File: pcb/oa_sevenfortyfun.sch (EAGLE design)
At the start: 33 parts, among them Q1 2N3904, Q10 2N3904, Q11 2N3904, Q12 2N3904, Q13 2N3904, Q14 2N3904, Q15 2N3906, Q16 2N3904, Q17 2N3906, Q18 2N3906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

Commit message: updating
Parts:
- added J1, J2, J3, J4, J5, J6, J7, J8: 1X01, Ai_Connectors:1X01
- added STANDOFF1, STANDOFF2, STANDOFF3, STANDOFF4: STAND-OFF, Ai_Electromechanical:STAND-OFF
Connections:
- removed net OFFSET1: Q6.E, R1.1
- removed net OFFSET2: Q7.E, R2.1
- new net NC: J8.1
- new net OFFSET_N1: J1.1, Q6.E, R1.1
- new net OFFSET_N2: J5.1, Q7.E, R2.1
- net IN+: now also J3.1
- net IN-: now also J2.1
- net OUT: now also J6.1
- net VCC+: now also J7.1
- net VCC-: now also J4.1
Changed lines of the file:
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@@
 <part name="R11" library="Ai_Passives" deviceset="RES" device="AXIAL-0.4"/>
 <part name="Q15" library="Ai_DiscreteSemis" deviceset="TRANSISTOR-PNP" device="" value="2N3906"/>
+<part name="STANDOFF1" library="Ai_Electromechanical" deviceset="STAND-OFF" device=""/>
+<part name="STANDOFF2" library="Ai_Electromechanical" deviceset="STAND-OFF" device=""/>
+<part name="STANDOFF3" library="Ai_Electromechanical" deviceset="STAND-OFF" device=""/>
+<part name="STANDOFF4" library="Ai_Electromechanical" deviceset="STAND-OFF" device=""/>
+<part name="J1" library="Ai_Connectors" deviceset="1X01" device=""/>
+<part name="J2" library="Ai_Connectors" deviceset="1X01" device=""/>
+<part name="J3" library="Ai_Connectors" deviceset="1X01" device=""/>
+<part name="J4" library="Ai_Connectors" deviceset="1X01" device=""/>
+<part name="J5" library="Ai_Connectors" deviceset="1X01" device=""/>
+<part name="J6" library="Ai_Connectors" deviceset="1X01" device=""/>
+<part name="J7" library="Ai_Connectors" deviceset="1X01" device=""/>
+<part name="J8" library="Ai_Connectors" deviceset="1X01" device=""/>
 </parts>
 <sheets>
@@
 <wire x1="168.91" y1="142.24" x2="168.91" y2="50.8" width="0.4064" layer="94" style="dashdot"/>
 <text x="62.23" y="144.78" size="1.778" layer="94" font="vector" ratio="15">DIFFERENTIAL AMPLIFIER</text>
-<text x="102.87" y="144.78" size="1.778" layer="94" font="vector" ratio="15">BIAS GENERATOR</text>
+<text x="106.68" y="144.78" size="1.778" layer="94" font="vector" ratio="15">BIAS GENERATOR</text>
 <text x="143.51" y="144.78" size="1.778" layer="94" font="vector" ratio="15">GAIN STAGE</text>
 <text x="171.45" y="144.78" size="1.778" layer="94" font="vector" ratio="15">OUTPUT STAGE</text>
@@
 <instance part="R11" gate="G$1" x="186.69" y="91.44" rot="R270"/>
 <instance part="Q15" gate="G$1" x="184.15" y="77.47" rot="MR0"/>
+<instance part="STANDOFF1" gate="G$1" x="132.08" y="2.54"/>
+<instance part="STANDOFF2" gate="G$1" x="137.16" y="2.54"/>
+<instance part="STANDOFF3" gate="G$1" x="142.24" y="2.54"/>
+<instance part="STANDOFF4" gate="G$1" x="127" y="2.54"/>
+<instance part="J1" gate="G$1" x="83.82" y="40.64" rot="R270"/>
+<instance part="J2" gate="G$1" x="107.95" y="40.64" rot="R270"/>
+<instance part="J3" gate="G$1" x="133.35" y="40.64" rot="R270"/>
+<instance part="J4" gate="G$1" x="158.75" y="40.64" rot="R270"/>
+<instance part="J5" gate="G$1" x="167.64" y="158.75" rot="R90"/>
+<instance part="J6" gate="G$1" x="146.05" y="158.75" rot="R90"/>
+<instance part="J7" gate="G$1" x="116.84" y="158.75" rot="R90"/>
+<instance part="J8" gate="G$1" x="90.17" y="158.75" rot="R90"/>
 </instances>
 <busses>
@@
 </segment>
 </net>
-<net name="OFFSET2" class="0">
+<net name="OFFSET_N2" class="0">
 <segment>
 <pinref part="Q7" gate="G$1" pin="E"/>
@@
 <label x="53.34" y="69.85" size="1.27" layer="95" font="vector" ratio="15" rot="R180" xref="yes"/>
 </segment>
-</net>
-<net name="OFFSET1" class="0">
-<segment>
-<pinref part="Q6" gate="G$1" pin="E"/>
-<pinref part="R1" gate="G$1" pin="1"/>
-<wire x1="64.77" y1="76.2" x2="64.77" y2="74.93" width="0.1524" layer="91"/>
-<wire x1="64.77" y1="74.93" x2="64.77" y2="68.58" width="0.1524" layer="91"/>
-<wire x1="64.77" y1="74.93" x2="53.34" y2="74.93" width="0.1524" layer="91"/>
-<junction x="64.77" y="74.93"/>
-<label x="53.34" y="74.93" size="1.27" layer="95" font="vector" ratio="15" rot="R180" xref="yes"/>
+<segment>
+<pinref part="J5" gate="G$1" pin="1"/>
+<wire x1="167.64" y1="163.83" x2="167.64" y2="166.37" width="0.1524" layer="91"/>
+<label x="167.64" y="166.37" size="1.27" layer="95" font="vector" ratio="15" rot="R90" xref="yes"/>
 </segment>
 </net>
@@
 <label x="53.34" y="116.84" size="1.27" layer="95" font="vector" ratio="15" rot="R180" xref="yes"/>
 </segment>
+<segment>
+<pinref part="J3" gate="G$1" pin="1"/>
+<wire x1="133.35" y1="35.56" x2="133.35" y2="33.02" width="0.1524" layer="91"/>
+<label x="133.35" y="33.02" size="1.27" layer="95" font="vector" ratio="15" rot="R270" xref="yes"/>
+</segment>
 </net>
 <net name="IN-" class="0">
@@
 <wire x1="96.52" y1="110.49" x2="53.34" y2="110.49" width="0.1524" layer="91"/>
 <label x="53.34" y="110.49" size="1.27" layer="95" font="vector" ratio="15" rot="R180" xref="yes"/>
+</segment>
+<segment>
+<pinref part="J2" gate="G$1" pin="1"/>
+<wire x1="107.95" y1="35.56" x2="107.95" y2="33.02" width="0.1524" layer="91"/>
+<label x="107.95" y="33.02" size="1.27" layer="95" font="vector" ratio="15" rot="R270" xref="yes"/>
 </segment>
 </net>
@@
 <junction x="186.69" y="85.09"/>
 <label x="196.85" y="85.09" size="1.27" layer="95" font="vector" ratio="15" xref="yes"/>
+</segment>
+<segment>
+<pinref part="J6" gate="G$1" pin="1"/>
+<wire x1="146.05" y1="163.83" x2="146.05" y2="166.37" width="0.1524" layer="91"/>
+<label x="146.05" y="166.37" size="1.27" layer="95" font="vector" ratio="15" rot="R90" xref="yes"/>
 </segment>
 </net>
@@
 <label x="53.34" y="54.61" size="1.27" layer="95" font="vector" ratio="15" rot="R180" xref="yes"/>
 </segment>
+<segment>
+<pinref part="J4" gate="G$1" pin="1"/>
+<wire x1="158.75" y1="35.56" x2="158.75" y2="33.02" width="0.1524" layer="91"/>
+<label x="158.75" y="33.02" size="1.27" layer="95" font="vector" ratio="15" rot="R270" xref="yes"/>
+</segment>
 </net>
 <net name="VCC+" class="0">
@@
 <label x="53.34" y="137.16" size="1.27" layer="95" font="vector" ratio="15" rot="R180" xref="yes"/>
 </segment>
-</net>
+<segment>
+<pinref part="J7" gate="G$1" pin="1"/>
+<wire x1="116.84" y1="163.83" x2="116.84" y2="166.37" width="0.1524" layer="91"/>
+<label x="116.84" y="166.37" size="1.27" layer="95" font="vector" ratio="15" rot="R90" xref="yes"/>
+</segment>
+</net>
+<net name="OFFSET_N1" class="0">
+<segment>
+<pinref part="J1" gate="G$1" pin="1"/>
+<wire x1="83.82" y1="35.56" x2="83.82" y2="33.02" width="0.1524" layer="91"/>
+<label x="83.82" y="33.02" size="1.27" layer="95" font="vector" ratio="15" rot="R270" xref="yes"/>
+</segment>
+<segment>
+<pinref part="Q6" gate="G$1" pin="E"/>
+<pinref part="R1" gate="G$1" pin="1"/>
+<wire x1="64.77" y1="76.2" x2="64.77" y2="74.93" width="0.1524" layer="91"/>
+<wire x1="64.77" y1="74.93" x2="64.77" y2="68.58" width="0.1524" layer="91"/>
+<wire x1="64.77" y1="74.93" x2="53.34" y2="74.93" width="0.1524" layer="91"/>
+<junction x="64.77" y="74.93"/>
+<label x="53.34" y="74.93" size="1.27" layer="95" font="vector" ratio="15" rot="R180" xref="yes"/>
+</segment>
+</net>
+<net name="NC" class="0">
+<segment>
+<pinref part="J8" gate="G$1" pin="1"/>
+<wire x1="90.17" y1="163.83" x2="90.17" y2="166.37" width="0.1524" layer="91"/>
+<label x="90.17" y="166.37" size="1.27" layer="95" font="vector" ratio="15" rot="R90" xref="yes"/>
+</segment>
+</net>

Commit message: Working on silkscreen
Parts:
- added J9: 2X04, Ai_Connectors:2X04
- J1, J2, J3, J4, J5, J6, J7, J8: value 1X01 -> 1X01-TERM; device Ai_Connectors:1X01 -> Ai_Connectors:1X01-TERM
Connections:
- net IN+: now also J9.5
- net IN-: now also J9.3
- net NC: now also J9.2
- net OFFSET_N1: now also J9.1
- net OFFSET_N2: now also J9.8
- net OUT: now also J9.6
- net VCC+: now also J9.4
- net VCC-: now also J9.7
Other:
- note added: "BREAKOUT"
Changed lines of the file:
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@@
 <?xml version="1.0" encoding="utf-8"?>
 <!DOCTYPE eagle SYSTEM "eagle.dtd">
-<eagle version="6.6.0">
+<eagle version="7.1.0">
 <drawing>
 <settings>
@@
 <part name="STANDOFF3" library="Ai_Electromechanical" deviceset="STAND-OFF" device=""/>
 <part name="STANDOFF4" library="Ai_Electromechanical" deviceset="STAND-OFF" device=""/>
-<part name="J1" library="Ai_Connectors" deviceset="1X01" device=""/>
-<part name="J2" library="Ai_Connectors" deviceset="1X01" device=""/>
-<part name="J3" library="Ai_Connectors" deviceset="1X01" device=""/>
-<part name="J4" library="Ai_Connectors" deviceset="1X01" device=""/>
-<part name="J5" library="Ai_Connectors" deviceset="1X01" device=""/>
-<part name="J6" library="Ai_Connectors" deviceset="1X01" device=""/>
-<part name="J7" library="Ai_Connectors" deviceset="1X01" device=""/>
-<part name="J8" library="Ai_Connectors" deviceset="1X01" device=""/>
+<part name="J1" library="Ai_Connectors" deviceset="1X01-TERM" device=""/>
+<part name="J2" library="Ai_Connectors" deviceset="1X01-TERM" device=""/>
+<part name="J3" library="Ai_Connectors" deviceset="1X01-TERM" device=""/>
+<part name="J4" library="Ai_Connectors" deviceset="1X01-TERM" device=""/>
+<part name="J5" library="Ai_Connectors" deviceset="1X01-TERM" device=""/>
+<part name="J6" library="Ai_Connectors" deviceset="1X01-TERM" device=""/>
+<part name="J7" library="Ai_Connectors" deviceset="1X01-TERM" device=""/>
+<part name="J8" library="Ai_Connectors" deviceset="1X01-TERM" device=""/>
+<part name="J9" library="Ai_Connectors" deviceset="2X04" device=""/>
 </parts>
 <sheets>
@@
 <wire x1="55.88" y1="142.24" x2="55.88" y2="50.8" width="0.4064" layer="94" style="dashdot"/>
 <wire x1="195.58" y1="142.24" x2="195.58" y2="50.8" width="0.4064" layer="94" style="dashdot"/>
+<text x="213.36" y="175.26" size="1.778" layer="94" font="vector" ratio="15">BREAKOUT</text>
 </plain>
 <instances>
@@
 <instance part="R11" gate="G$1" x="186.69" y="91.44" rot="R270"/>
 <instance part="Q15" gate="G$1" x="184.15" y="77.47" rot="MR0"/>
-<instance part="STANDOFF1" gate="G$1" x="132.08" y="2.54"/>
-<instance part="STANDOFF2" gate="G$1" x="137.16" y="2.54"/>
-<instance part="STANDOFF3" gate="G$1" x="142.24" y="2.54"/>
-<instance part="STANDOFF4" gate="G$1" x="127" y="2.54"/>
-<instance part="J1" gate="G$1" x="83.82" y="40.64" rot="R270"/>
-<instance part="J2" gate="G$1" x="107.95" y="40.64" rot="R270"/>
-<instance part="J3" gate="G$1" x="133.35" y="40.64" rot="R270"/>
-<instance part="J4" gate="G$1" x="158.75" y="40.64" rot="R270"/>
-<instance part="J5" gate="G$1" x="167.64" y="158.75" rot="R90"/>
-<instance part="J6" gate="G$1" x="146.05" y="158.75" rot="R90"/>
+<instance part="STANDOFF1" gate="G$1" x="132.08" y="15.24"/>
+<instance part="STANDOFF2" gate="G$1" x="125.73" y="8.89"/>
+<instance part="STANDOFF3" gate="G$1" x="132.08" y="8.89"/>
+<instance part="STANDOFF4" gate="G$1" x="125.73" y="15.24"/>
+<instance part="J1" gate="G$1" x="76.2" y="40.64" rot="R270"/>
+<instance part="J2" gate="G$1" x="116.84" y="40.64" rot="R270"/>
+<instance part="J3" gate="G$1" x="151.13" y="40.64" rot="R270"/>
+<instance part="J4" gate="G$1" x="181.61" y="40.64" rot="R270"/>
+<instance part="J5" gate="G$1" x="181.61" y="158.75" rot="R90"/>
+<instance part="J6" gate="G$1" x="151.13" y="158.75" rot="R90"/>
 <instance part="J7" gate="G$1" x="116.84" y="158.75" rot="R90"/>
-<instance part="J8" gate="G$1" x="90.17" y="158.75" rot="R90"/>
+<instance part="J8" gate="G$1" x="76.2" y="158.75" rot="R90"/>
+<instance part="J9" gate="G$1" x="218.44" y="166.37" rot="MR0"/>
 </instances>
 <busses>
@@
 <segment>
 <pinref part="J5" gate="G$1" pin="1"/>
-<wire x1="167.64" y1="163.83" x2="167.64" y2="166.37" width="0.1524" layer="91"/>
-<label x="167.64" y="166.37" size="1.27" layer="95" font="vector" ratio="15" rot="R90" xref="yes"/>
+<wire x1="181.61" y1="158.75" x2="181.61" y2="166.37" width="0.1524" layer="91"/>
+<label x="181.61" y="166.37" size="1.27" layer="95" font="vector" ratio="15" rot="R90" xref="yes"/>
+</segment>
+<segment>
+<pinref part="J9" gate="G$1" pin="8"/>
+<wire x1="226.06" y1="168.91" x2="228.6" y2="168.91" width="0.1524" layer="91"/>
+<label x="228.6" y="168.91" size="1.27" layer="95" font="vector" ratio="15" xref="yes"/>
 </segment>
 </net>
@@
 <segment>
 <pinref part="J3" gate="G$1" pin="1"/>
-<wire x1="133.35" y1="35.56" x2="133.35" y2="33.02" width="0.1524" layer="91"/>
-<label x="133.35" y="33.02" size="1.27" layer="95" font="vector" ratio="15" rot="R270" xref="yes"/>
+<wire x1="151.13" y1="40.64" x2="151.13" y2="33.02" width="0.1524" layer="91"/>
+<label x="151.13" y="33.02" size="1.27" layer="95" font="vector" ratio="15" rot="R270" xref="yes"/>
+</segment>
+<segment>
+<pinref part="J9" gate="G$1" pin="5"/>
+<wire x1="210.82" y1="166.37" x2="208.28" y2="166.37" width="0.1524" layer="91"/>
+<label x="208.28" y="166.37" size="1.27" layer="95" font="vector" ratio="15" rot="R180" xref="yes"/>
 </segment>
 </net>
@@
 <segment>
 <pinref part="J2" gate="G$1" pin="1"/>
-<wire x1="107.95" y1="35.56" x2="107.95" y2="33.02" width="0.1524" layer="91"/>
-<label x="107.95" y="33.02" size="1.27" layer="95" font="vector" ratio="15" rot="R270" xref="yes"/>
+<wire x1="116.84" y1="40.64" x2="116.84" y2="33.02" width="0.1524" layer="91"/>
+<label x="116.84" y="33.02" size="1.27" layer="95" font="vector" ratio="15" rot="R270" xref="yes"/>
+</segment>
+<segment>
+<pinref part="J9" gate="G$1" pin="3"/>
+<wire x1="210.82" y1="163.83" x2="208.28" y2="163.83" width="0.1524" layer="91"/>
+<label x="208.28" y="163.83" size="1.27" layer="95" font="vector" ratio="15" rot="R180" xref="yes"/>
 </segment>
 </net>
@@
 <segment>
 <pinref part="J6" gate="G$1" pin="1"/>
-<wire x1="146.05" y1="163.83" x2="146.05" y2="166.37" width="0.1524" layer="91"/>
-<label x="146.05" y="166.37" size="1.27" layer="95" font="vector" ratio="15" rot="R90" xref="yes"/>
+<wire x1="151.13" y1="158.75" x2="151.13" y2="166.37" width="0.1524" layer="91"/>
+<label x="151.13" y="166.37" size="1.27" layer="95" font="vector" ratio="15" rot="R90" xref="yes"/>
+</segment>
+<segment>
+<pinref part="J9" gate="G$1" pin="6"/>
+<wire x1="226.06" y1="166.37" x2="228.6" y2="166.37" width="0.1524" layer="91"/>
+<label x="228.6" y="166.37" size="1.27" layer="95" font="vector" ratio="15" xref="yes"/>
 </segment>
 </net>
@@
 <segment>
 <pinref part="J4" gate="G$1" pin="1"/>
-<wire x1="158.75" y1="35.56" x2="158.75" y2="33.02" width="0.1524" layer="91"/>
-<label x="158.75" y="33.02" size="1.27" layer="95" font="vector" ratio="15" rot="R270" xref="yes"/>
+<wire x1="181.61" y1="40.64" x2="181.61" y2="33.02" width="0.1524" layer="91"/>
+<label x="181.61" y="33.02" size="1.27" layer="95" font="vector" ratio="15" rot="R270" xref="yes"/>
+</segment>
+<segment>
+<pinref part="J9" gate="G$1" pin="7"/>
+<wire x1="210.82" y1="168.91" x2="208.28" y2="168.91" width="0.1524" layer="91"/>
+<label x="208.28" y="168.91" size="1.27" layer="95" font="vector" ratio="15" rot="R180" xref="yes"/>
 </segment>
 </net>
@@
 <segment>
 <pinref part="J7" gate="G$1" pin="1"/>
-<wire x1="116.84" y1="163.83" x2="116.84" y2="166.37" width="0.1524" layer="91"/>
+<wire x1="116.84" y1="158.75" x2="116.84" y2="166.37" width="0.1524" layer="91"/>
 <label x="116.84" y="166.37" size="1.27" layer="95" font="vector" ratio="15" rot="R90" xref="yes"/>
 </segment>
+<segment>
+<pinref part="J9" gate="G$1" pin="4"/>
+<wire x1="226.06" y1="163.83" x2="228.6" y2="163.83" width="0.1524" layer="91"/>
+<label x="228.6" y="163.83" size="1.27" layer="95" font="vector" ratio="15" xref="yes"/>
+</segment>
 </net>
 <net name="OFFSET_N1" class="0">
 <segment>
 <pinref part="J1" gate="G$1" pin="1"/>
-<wire x1="83.82" y1="35.56" x2="83.82" y2="33.02" width="0.1524" layer="91"/>
-<label x="83.82" y="33.02" size="1.27" layer="95" font="vector" ratio="15" rot="R270" xref="yes"/>
+<wire x1="76.2" y1="40.64" x2="76.2" y2="33.02" width="0.1524" layer="91"/>
+<label x="76.2" y="33.02" size="1.27" layer="95" font="vector" ratio="15" rot="R270" xref="yes"/>
 </segment>
 <segment>
@@
 <label x="53.34" y="74.93" size="1.27" layer="95" font="vector" ratio="15" rot="R180" xref="yes"/>
 </segment>
+<segment>
+<pinref part="J9" gate="G$1" pin="1"/>
+<wire x1="210.82" y1="161.29" x2="208.28" y2="161.29" width="0.1524" layer="91"/>
+<label x="208.28" y="161.29" size="1.27" layer="95" font="vector" ratio="15" rot="R180" xref="yes"/>
+</segment>
 </net>
 <net name="NC" class="0">
 <segment>
 <pinref part="J8" gate="G$1" pin="1"/>
-<wire x1="90.17" y1="163.83" x2="90.17" y2="166.37" width="0.1524" layer="91"/>
-<label x="90.17" y="166.37" size="1.27" layer="95" font="vector" ratio="15" rot="R90" xref="yes"/>
-</segment>
-</net>
+<wire x1="76.2" y1="158.75" x2="76.2" y2="166.37" width="0.1524" layer="91"/>
+<label x="76.2" y="166.37" size="1.27" layer="95" font="vector" ratio="15" rot="R90" xref="yes"/>
+</segment>
+<segment>
+<pinref part="J9" gate="G$1" pin="2"/>
+<wire x1="226.06" y1="161.29" x2="228.6" y2="161.29" width="0.1524" layer="91"/>
+<label x="228.6" y="161.29" size="1.27" layer="95" font="vector" ratio="15" xref="yes"/>
+</segment>
+</net>

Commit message: starting to route
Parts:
- C1: value (none) -> 30pF
- J9: value 2X04 -> 2X04SHR; device Ai_Connectors:2X04 -> Ai_Connectors:2X04SHR
- R1, R2: value (none) -> 1K
- R10: value (none) -> 25
- R11, R9: value (none) -> 50
- R3, R8: value (none) -> 50K
- R4: value (none) -> 5K
- R5: value (none) -> 39K
- R6: value (none) -> 4.5K
- R7: value (none) -> 7.5K
- U$3: value AI-LOGOXS -> AI-LOGOL; device Ai_Miscellany:AI-LOGOXS -> Ai_Miscellany:AI-LOGOL
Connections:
- removed net N$23: Q12.C, Q16.E
- removed net N$25: Q14.E, R10.2, R11.1
- new net N$7: Q15.E, R11.2
- net N$18: now also Q12.C, Q15.B, Q16.E
- net OUT: now also Q14.E, R10.2, R11.1; no longer Q15.E, R11.2
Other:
- moved on the sheet: Q10, Q12, Q15, Q6, Q7, R10, R11

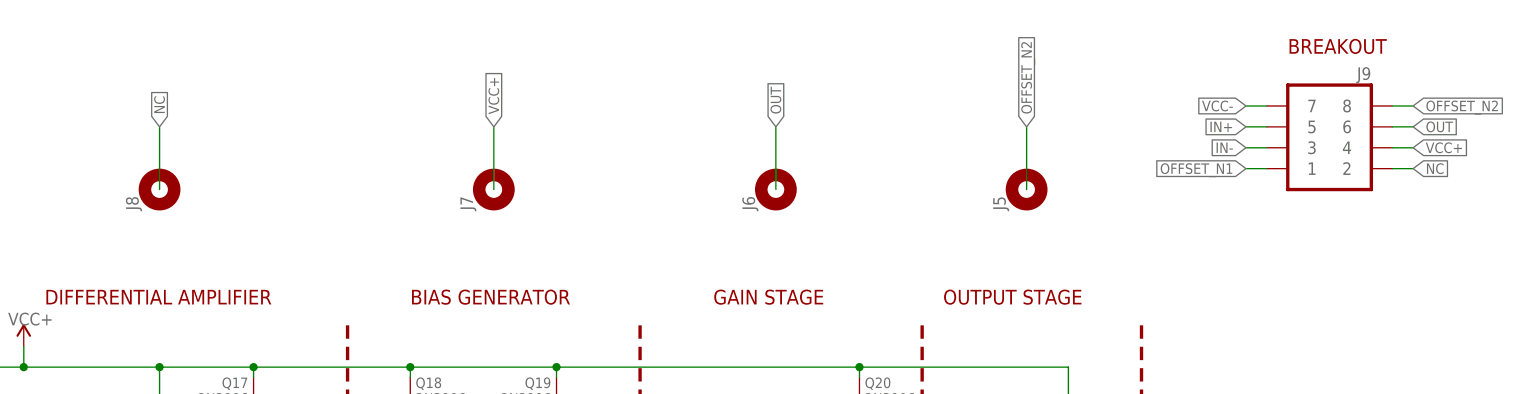
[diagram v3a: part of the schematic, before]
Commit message: Routed. Worked on silkscreen.
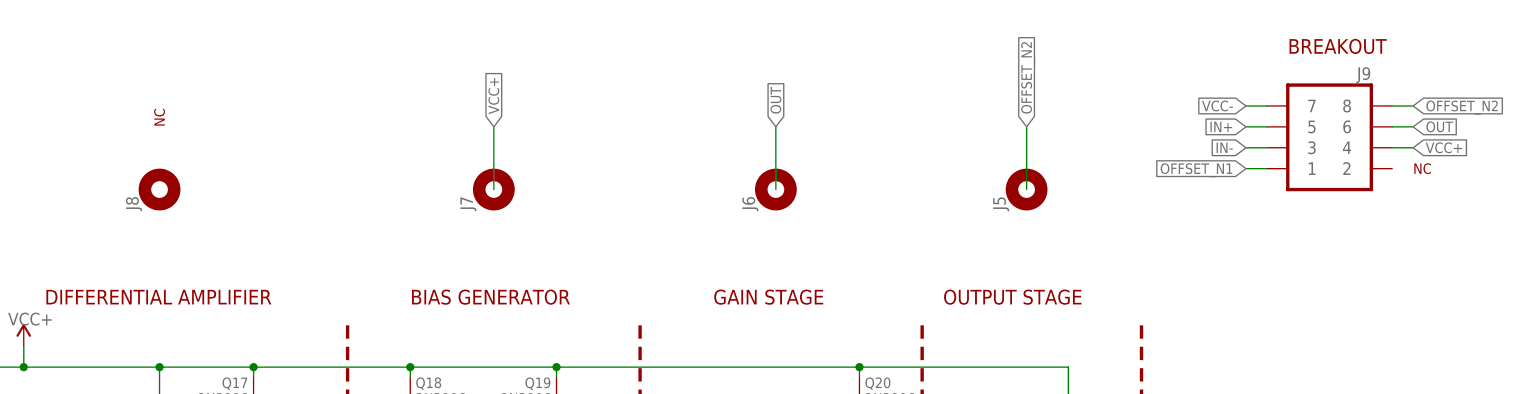
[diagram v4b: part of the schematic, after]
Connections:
- removed net NC: J8.1, J9.2
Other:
- note added: "NC"
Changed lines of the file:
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@@
 <setting verticaltext="up"/>
 </settings>
-<grid distance="50" unitdist="mil" unit="mil" style="lines" multiple="1" display="yes" altdistance="0.01" altunitdist="inch" altunit="inch"/>
+<grid distance="25" unitdist="mil" unit="mil" style="lines" multiple="1" display="yes" altdistance="0.01" altunitdist="inch" altunit="inch"/>
 <layers>
 <layer number="1" name="Top" color="4" fill="1" visible="no" active="no"/>
@@
 <wire x1="195.58" y1="142.24" x2="195.58" y2="50.8" width="0.4064" layer="94" style="dashdot"/>
 <text x="213.36" y="175.26" size="1.778" layer="94" font="vector" ratio="15">BREAKOUT</text>
+<text x="228.6" y="160.655" size="1.27" layer="94" font="vector" ratio="15">NC</text>
+<text x="76.835" y="166.37" size="1.27" layer="94" font="vector" ratio="15" rot="R90">NC</text>
 </plain>
 <instances>
@@
 </segment>
 </net>
-<net name="NC" class="0">
-<segment>
-<pinref part="J8" gate="G$1" pin="1"/>
-<wire x1="76.2" y1="158.75" x2="76.2" y2="166.37" width="0.1524" layer="91"/>
-<label x="76.2" y="166.37" size="1.27" layer="95" font="vector" ratio="15" rot="R90" xref="yes"/>
-</segment>
-<segment>
-<pinref part="J9" gate="G$1" pin="2"/>
-<wire x1="226.06" y1="161.29" x2="228.6" y2="161.29" width="0.1524" layer="91"/>
-<label x="228.6" y="161.29" size="1.27" layer="95" font="vector" ratio="15" xref="yes"/>
-</segment>
-</net>
 <net name="N$7" class="0">
 <segment>
@@
 </sheet>
 </sheets>
+<errors>
+</errors>
 </schematic>
 </drawing>
